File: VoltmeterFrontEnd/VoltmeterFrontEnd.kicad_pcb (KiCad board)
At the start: 4 copper layers, 46 x 24.4 mm, 20 parts, among them J1 Voltmeter, J15 Barrel_Jack, Q8 AO3400A MOSFET, SW3 SW_Push, U10 LM4040DBZ-2.5, U4 IX4426N, U7 MAX1683

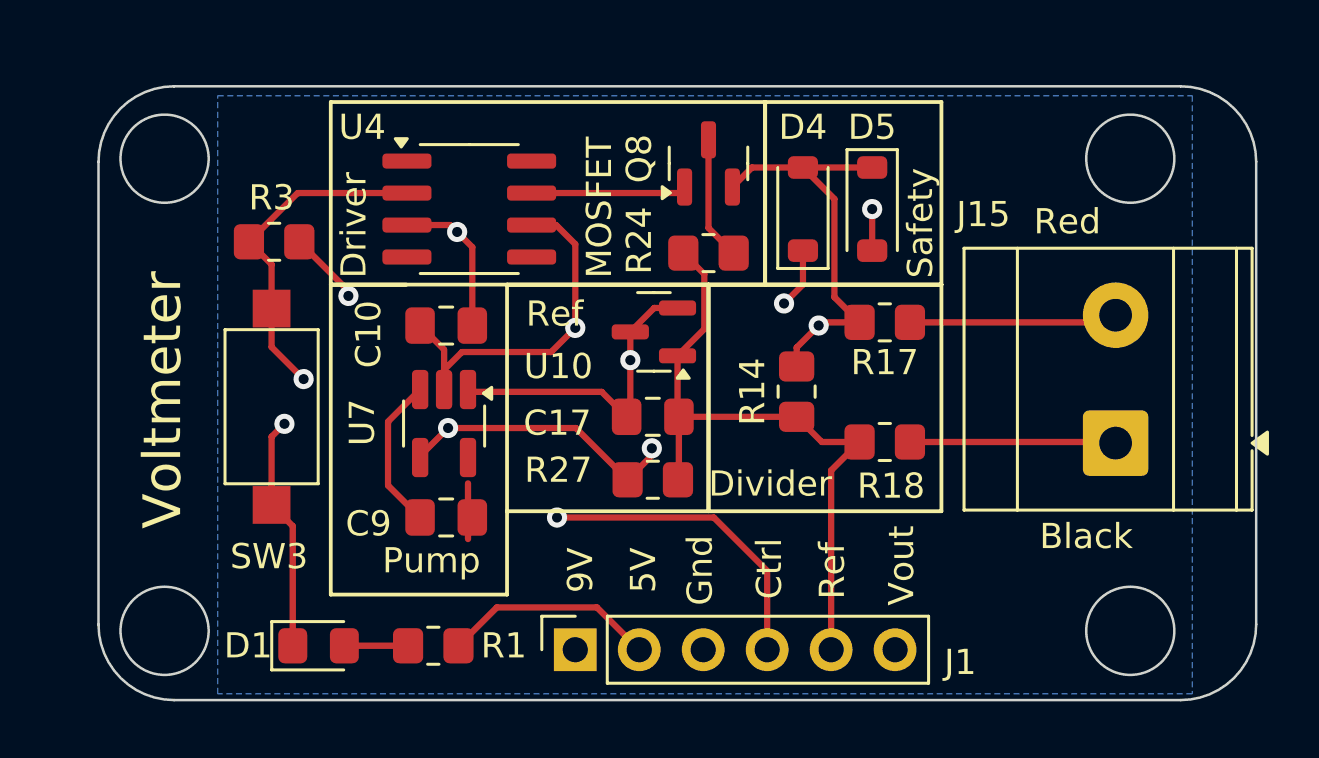
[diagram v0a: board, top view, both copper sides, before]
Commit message: Finishing PCBs to be made.
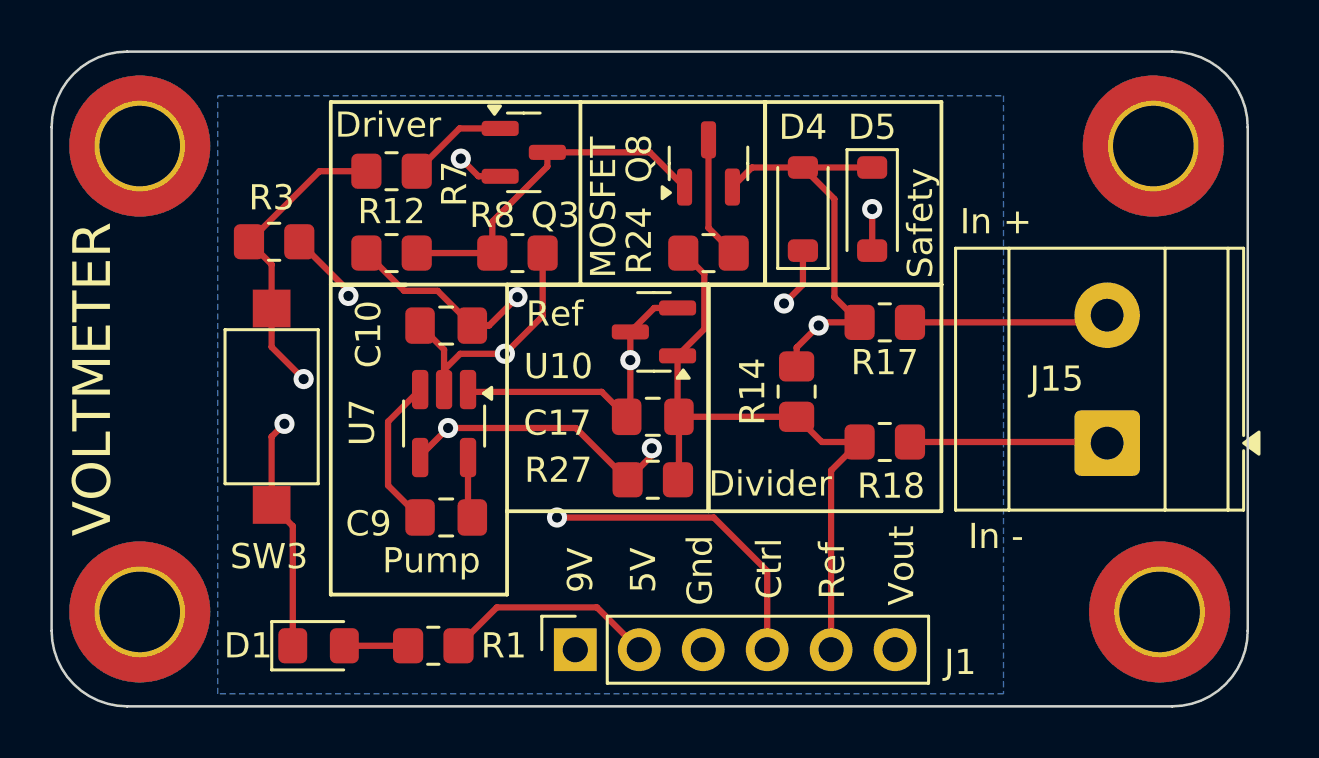
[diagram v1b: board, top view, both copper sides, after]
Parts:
- removed U4: IX4426N, Package_SO:SOIC-8_3.9x4.9mm_P1.27mm
- added H1: MountingHole, MountingHole:MountingHole_3.2mm_M3_DIN965_Pad_TopBottom, F.Cu at (94.0, 65.5)
- added H2: MountingHole, MountingHole:MountingHole_3.2mm_M3_DIN965_Pad_TopBottom, F.Cu at (134.2, 65.5)
- added H3: MountingHole, MountingHole:MountingHole_3.2mm_M3_DIN965_Pad_TopBottom, F.Cu at (134.5, 84.0)
- added H4: MountingHole, MountingHole:MountingHole_3.2mm_M3_DIN965_Pad_TopBottom, F.Cu at (94.0, 84.0)
- added Q3: MMBT3904, Package_TO_SOT_SMD:SOT-23, F.Cu at (109.2, 65.8)
- added R12: 100K, Resistor_SMD:R_0805_2012Metric_Pad1.20x1.40mm_HandSolder, F.Cu at (104.0, 69.8)
- added R7: 22K, Resistor_SMD:R_0805_2012Metric_Pad1.20x1.40mm_HandSolder, F.Cu at (104.0, 66.5)
- added R8: 10K, Resistor_SMD:R_0805_2012Metric_Pad1.20x1.40mm_HandSolder, F.Cu at (109.0, 69.8)
- R3: value 1K -> 10K
- moved J15 0.34 mm to (132.4, 77.3)
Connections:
- net VmeterMOSFET renamed MOSFET_Ctrl
- Q8 pad 1: /Driver_U4_Out_A -> /MOSFET_Gate
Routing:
- net /MOSFET_Gate: track 0.00 -> 13.9 mm
- net /Driver_U4_Out_A: track 6.17 -> 0.00 mm
- net Net-(Q3-B): track 0.00 -> 4.02 mm
- net +9V: track 27.8 -> 23.9 mm
- net GND: track 29.5 -> 32.6 mm, vias 4 -> 5
- net MOSFET_Ctrl: track 38.1 -> 36.9 mm
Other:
- board size 46 x 24.4 mm -> 47.5 x 26 mm
- board text added: "18.5mm"
- board text added: "40.5mm"
- board text added: "In +"
- board text added: "In -"
- board text added: "OIH Designs | Voltmeter Front End: V1 Above Ground Bias w Open Lead Detect Vout = (+Vin/((R17+18)/R14))-VRef) Populate either charge pump or supply ~9vdc. Not Both. Input safe voltages only w/o extra precautions & testing."
- board text added: "SN"
- board text added: "VOLTMETER"
- board text removed: "Black"
- board text removed: "OIH Designs Voltmeter Breakout V1"
- board text removed: "Red"
- board text removed: "Voltmeter"
- board text removed: "Voltmeter Front End: Above Gnd w Open Lead Detect Populate Charge pump or supply ~9vdc. Not Both. Input safe voltages only w/o extra precautions & testing."
